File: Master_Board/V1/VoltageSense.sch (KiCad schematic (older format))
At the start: 3 parts

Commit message: git modify Master_board
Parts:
- removed U?: OP-AMP, F, symbol OP-AMP
- added C? (x4): 885012207098, Capacitors:C0805, symbol 885012207098
- added C? (x6): 885012207080, Capacitors:C0805, symbol 885012207080
- added D?: Diode, F, symbol Diode
- added J? (x2): 649002227222, Connectors:649002227222, symbol 649002227222
- added R? (x10): RC0805JR-0710KL, Resistors:R0805, symbol RC0805JR-0710KL
- added R? (x2): RC0805JR-071ML, Resistors:R0805, symbol RC0805JR-071ML
- added U? (x2): ACPL-C87A-500E, F, symbol ACPL-C87A-500E
- added U? (x2): LMV321RILT, IC:SOT-23-5, symbol LMV321RILT
- added U?: NCS1S2405SC, IC:MSOP-8-EP, symbol NCS1S2405SC
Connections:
- net labels added: 12V, 3.3V, 5V, 5V_ISO, BP-HV+, BP-HV-, BP_VSense, DGND, MPPT-HV+, MPPT-HV-, MPPT_VSense, VSense_EN
- net labels removed: HV+, HV-
- wire segments 2 -> 100
- no-connect marks 2 -> 4
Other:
- note added: "TODO: LC filter + control"
- moved on the sheet: J?

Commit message: Add filter in VoltageSense
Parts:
- added C?: 885012207075, Capacitors:C0805, symbol 885012207075
- added L?: RLB0608-471KL, Inductors:RLB0608, symbol RLB0608-471KL
- added R?: RC0805JR-07470RL, Resistors:R0805, symbol RC0805JR-07470RL
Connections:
- wire segments 100 -> 129
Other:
- note added: "Isolated"
- note removed: "TODO: LC filter + control"

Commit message: Add page LedDriver
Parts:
- gave numbers to parts that had none: 35
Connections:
- wire segments 129 -> 106

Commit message: Modify MasterBoard.sch
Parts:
- removed D801: Diode, F, symbol Diode
- removed R809, R810, R812, R813: RC0805JR-0710KL, Resistors:R0805, symbol RC0805JR-0710KL
- added D?: SD0805S020S1R0, Diodes:Diode_0805, symbol SD0805S020S1R0
- added R? (x4): RC0805JR-0715KL, Resistors:R0805, symbol RC0805JR-0715KL
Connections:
- wire segments 106 -> 104

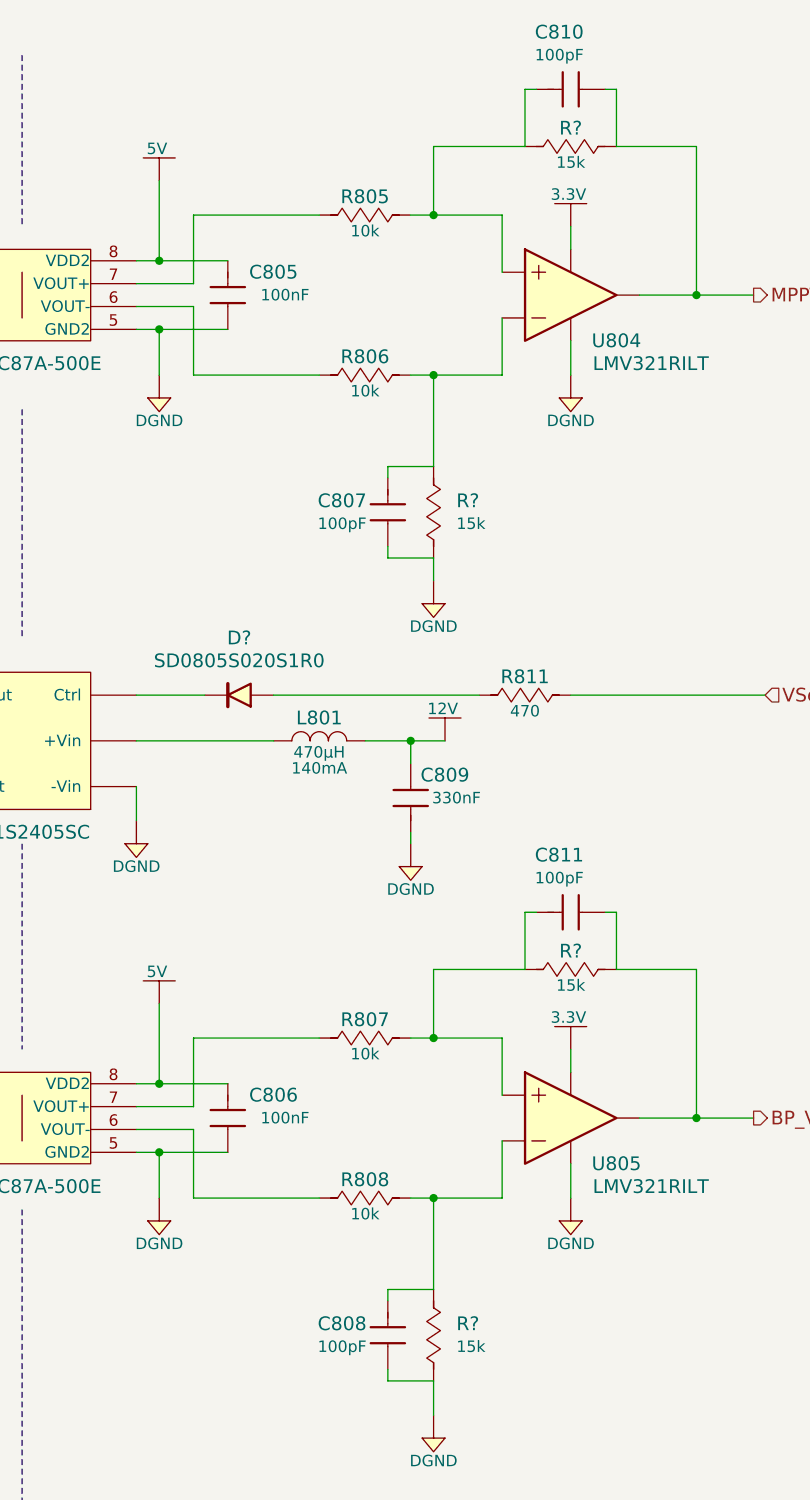
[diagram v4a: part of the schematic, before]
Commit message: Add page LEDDriver.sch
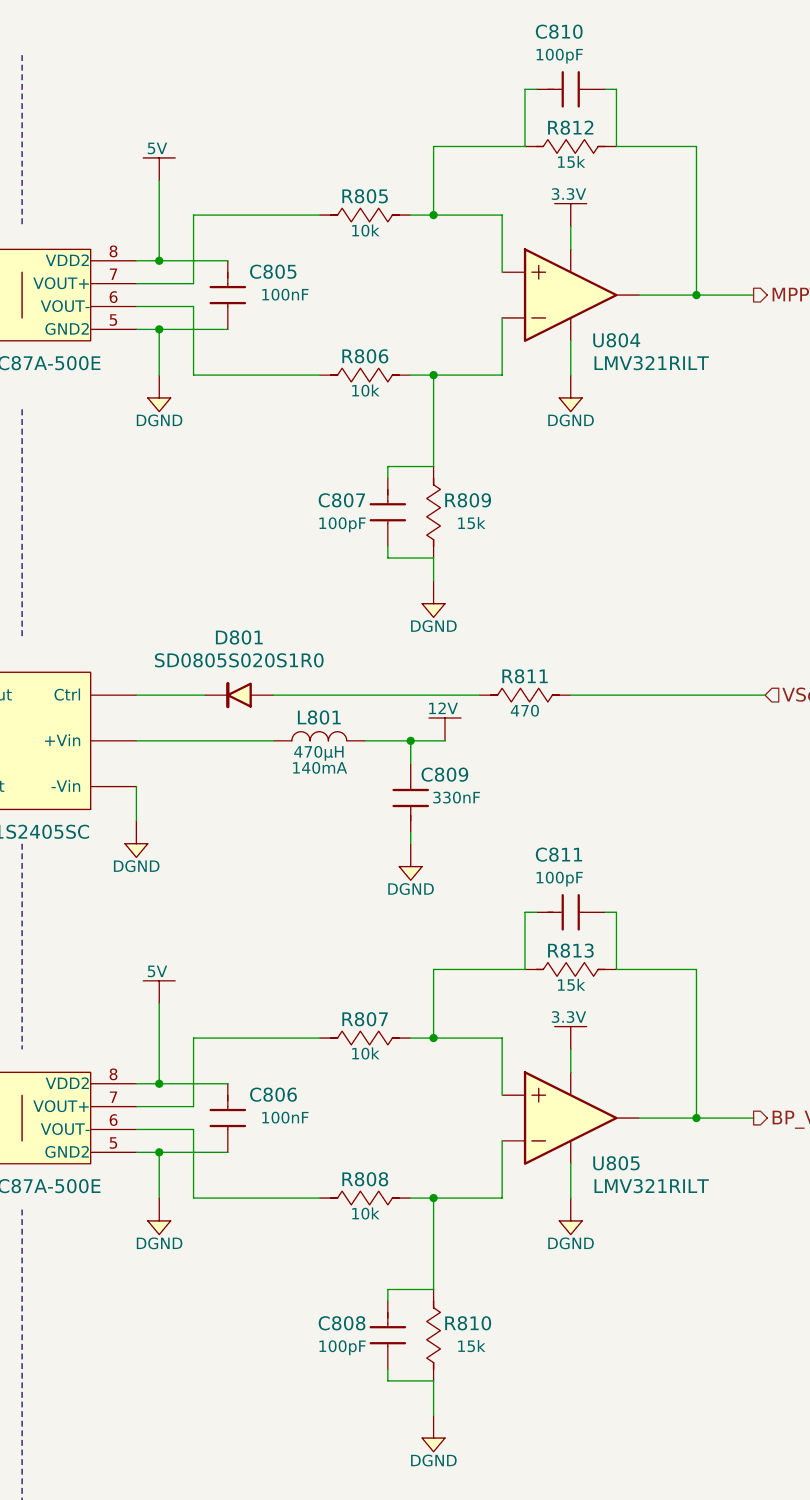
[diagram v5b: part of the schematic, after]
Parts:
- U801, U803: footprint F -> IC:SSO-8
- gave numbers to parts that had none: 5
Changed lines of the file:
@@
 EESchema Schematic File Version 2
-LIBS:Master_Board-rescue
 LIBS:ADC
 LIBS:Amplifiers
@@
 NoConn ~ 2100 5950
 $Comp
-L ACPL-C87A-500E U803
-U 1 1 5949C11F
-P 4900 5500
-F 0 "U803" H 4650 6000 60  0000 C CNN
-F 1 "ACPL-C87A-500E" H 4900 5400 60  0000 C CNN
-F 2 "F" H 4900 4600 60  0001 C CNN
-F 3 "https://docs.broadcom.com/docs/AV02-3563EN" H 4900 4500 60  0001 C CNN
-F 4 "Digikey" H 4900 5100 60  0001 C CNN "Supplier"
-F 5 "516-3140-1-ND" H 4900 5000 60  0001 C CNN "Supplier Part Number"
-F 6 "Broadcom Limited" H 4900 4900 60  0001 C CNN "Manufacturer"
-F 7 "ACPL-C87A-500E" H 4900 4800 60  0001 C CNN "Manufacturer Part Number"
-F 8 "Precision Optically Isolated Voltage Sensor" H 4900 4700 60  0001 C CNN "Description"
-	1    4900 5500
-	1    0    0    -1
-$EndComp
-$Comp
-L DGND #PWR802
+L DGND #PWR087
 U 1 1 5949C551
 P 4300 5700
-F 0 "#PWR802" H 4300 5530 50  0001 C CNN
+F 0 "#PWR087" H 4300 5530 50  0001 C CNN
 F 1 "DGND" H 4300 5600 50  0000 C CNN
 F 2 "" H 4300 5800 60  0000 C CNN
@@
 $EndComp
 $Comp
-L DGND #PWR808
+L DGND #PWR088
 U 1 1 5949C56B
 P 5500 5750
-F 0 "#PWR808" H 5500 5580 50  0001 C CNN
+F 0 "#PWR088" H 5500 5580 50  0001 C CNN
 F 1 "DGND" H 5500 5650 50  0000 C CNN
 F 2 "" H 5500 5850 60  0000 C CNN
@@
 BP_VSense
 $Comp
-L DGND #PWR816
+L DGND #PWR089
 U 1 1 5949FCE5
 P 7300 5750
-F 0 "#PWR816" H 7300 5580 50  0001 C CNN
+F 0 "#PWR089" H 7300 5580 50  0001 C CNN
 F 1 "DGND" H 7300 5650 50  0000 C CNN
 F 2 "" H 7300 5850 60  0000 C CNN
@@
 $EndComp
 $Comp
-L DGND #PWR811
+L DGND #PWR090
 U 1 1 594A0EB3
 P 6700 6700
-F 0 "#PWR811" H 6700 6530 50  0001 C CNN
+F 0 "#PWR090" H 6700 6530 50  0001 C CNN
 F 1 "DGND" H 6700 6600 50  0000 C CNN
 F 2 "" H 6700 6800 60  0000 C CNN
@@
 $EndComp
 $Comp
-L 5V #PWR807
+L 5V #PWR091
 U 1 1 594A3B0E
 P 5500 4800
-F 0 "#PWR807" H 5500 4650 50  0001 C CNN
+F 0 "#PWR091" H 5500 4650 50  0001 C CNN
 F 1 "5V" H 5490 4940 50  0000 C CNN
 F 2 "" H 5500 4800 60  0000 C CNN
@@
 $EndComp
 $Comp
-L 3.3V #PWR815
+L 3.3V #PWR092
 U 1 1 594A4CD5
 P 7300 5000
-F 0 "#PWR815" H 7300 4850 50  0001 C CNN
+F 0 "#PWR092" H 7300 4850 50  0001 C CNN
 F 1 "3.3V" H 7290 5140 50  0000 C CNN
 F 2 "" H 7300 5000 60  0000 C CNN
@@
 $EndComp
 $Comp
-L DGND #PWR803
+L DGND #PWR093
 U 1 1 594A764A
 P 4400 4100
-F 0 "#PWR803" H 4400 3930 50  0001 C CNN
+F 0 "#PWR093" H 4400 3930 50  0001 C CNN
 F 1 "DGND" H 4400 4000 50  0000 C CNN
 F 2 "" H 4400 4200 60  0000 C CNN
@@
 $EndComp
 $Comp
-L DGND #PWR804
+L DGND #PWR094
 U 1 1 594A76E3
 P 5400 4100
-F 0 "#PWR804" H 5400 3930 50  0001 C CNN
+F 0 "#PWR094" H 5400 3930 50  0001 C CNN
 F 1 "DGND" H 5400 4000 50  0000 C CNN
 F 2 "" H 5400 4200 60  0000 C CNN
@@
 $EndComp
 $Comp
-L 12V #PWR812
+L 12V #PWR095
 U 1 1 594A78A1
 P 6750 3650
-F 0 "#PWR812" H 6750 3500 50  0001 C CNN
+F 0 "#PWR095" H 6750 3500 50  0001 C CNN
 F 1 "12V" H 6740 3790 50  0000 C CNN
 F 2 "" H 6750 3650 60  0000 C CNN
@@
 NoConn ~ 2100 2350
 $Comp
-L ACPL-C87A-500E U801
-U 1 1 594A8989
-P 4900 1900
-F 0 "U801" H 4650 2400 60  0000 C CNN
-F 1 "ACPL-C87A-500E" H 4900 1800 60  0000 C CNN
-F 2 "F" H 4900 1000 60  0001 C CNN
-F 3 "https://docs.broadcom.com/docs/AV02-3563EN" H 4900 900 60  0001 C CNN
-F 4 "Digikey" H 4900 1500 60  0001 C CNN "Supplier"
-F 5 "516-3140-1-ND" H 4900 1400 60  0001 C CNN "Supplier Part Number"
-F 6 "Broadcom Limited" H 4900 1300 60  0001 C CNN "Manufacturer"
-F 7 "ACPL-C87A-500E" H 4900 1200 60  0001 C CNN "Manufacturer Part Number"
-F 8 "Precision Optically Isolated Voltage Sensor" H 4900 1100 60  0001 C CNN "Description"
-	1    4900 1900
-	1    0    0    -1
-$EndComp
-$Comp
-L DGND #PWR801
+L DGND #PWR096
 U 1 1 594A898F
 P 4300 2100
-F 0 "#PWR801" H 4300 1930 50  0001 C CNN
+F 0 "#PWR096" H 4300 1930 50  0001 C CNN
 F 1 "DGND" H 4300 2000 50  0000 C CNN
 F 2 "" H 4300 2200 60  0000 C CNN
@@
 $EndComp
 $Comp
-L DGND #PWR806
+L DGND #PWR097
 U 1 1 594A8995
 P 5500 2150
-F 0 "#PWR806" H 5500 1980 50  0001 C CNN
+F 0 "#PWR097" H 5500 1980 50  0001 C CNN
 F 1 "DGND" H 5500 2050 50  0000 C CNN
 F 2 "" H 5500 2250 60  0000 C CNN
@@
 MPPT_VSense
 $Comp
-L DGND #PWR814
+L DGND #PWR098
 U 1 1 594A8A41
 P 7300 2150
-F 0 "#PWR814" H 7300 1980 50  0001 C CNN
+F 0 "#PWR098" H 7300 1980 50  0001 C CNN
 F 1 "DGND" H 7300 2050 50  0000 C CNN
 F 2 "" H 7300 2250 60  0000 C CNN
@@
 $EndComp
 $Comp
-L DGND #PWR810
+L DGND #PWR099
 U 1 1 594A8A81
 P 6700 3050
-F 0 "#PWR810" H 6700 2880 50  0001 C CNN
+F 0 "#PWR099" H 6700 2880 50  0001 C CNN
 F 1 "DGND" H 6700 2950 50  0000 C CNN
 F 2 "" H 6700 3150 60  0000 C CNN
@@
 $EndComp
 $Comp
-L 5V #PWR805
+L 5V #PWR0100
 U 1 1 594A8A88
 P 5500 1200
-F 0 "#PWR805" H 5500 1050 50  0001 C CNN
+F 0 "#PWR0100" H 5500 1050 50  0001 C CNN
 F 1 "5V" H 5490 1340 50  0000 C CNN
 F 2 "" H 5500 1200 60  0000 C CNN
@@
 $EndComp
 $Comp
-L 3.3V #PWR813
+L 3.3V #PWR0101
 U 1 1 594A8A8E
 P 7300 1400
-F 0 "#PWR813" H 7300 1250 50  0001 C CNN
+F 0 "#PWR0101" H 7300 1250 50  0001 C CNN
 F 1 "3.3V" H 7290 1540 50  0000 C CNN
 F 2 "" H 7300 1400 60  0000 C CNN
@@
 Connection ~ 6600 3650
 $Comp
-L DGND #PWR809
+L DGND #PWR0102
 U 1 1 59486B2F
 P 6600 4200
-F 0 "#PWR809" H 6600 4030 50  0001 C CNN
+F 0 "#PWR0102" H 6600 4030 50  0001 C CNN
 F 1 "DGND" H 6600 4100 50  0000 C CNN
 F 2 "" H 6600 4300 60  0000 C CNN
@@
 Isolated
 $Comp
-L SD0805S020S1R0 D?
+L SD0805S020S1R0 D801
 U 1 1 594E14E6
 P 5800 3450
-F 0 "D?" H 5750 3200 60  0000 C CNN
+F 0 "D801" H 5750 3200 60  0000 C CNN
 F 1 "SD0805S020S1R0" H 5750 3300 60  0000 C CNN
 F 2 "Diodes:Diode_0805" H 5800 2430 60  0001 C CNN
@@
 $EndComp
 $Comp
-L RC0805JR-0715KL R?
+L RC0805JR-0715KL R812
 U 1 1 59539105
 P 7300 1050
-F 0 "R?" H 7300 1130 60  0000 C CNN
+F 0 "R812" H 7300 1130 60  0000 C CNN
 F 1 "RC0805JR-0715KL" H 7300 750 50  0001 C CNN
 F 2 "Resistors:R0805" H 7300 150 30  0001 C CNN
@@
 $EndComp
 $Comp
-L RC0805JR-0715KL R?
+L RC0805JR-0715KL R813
 U 1 1 59539316
 P 7300 4650
-F 0 "R?" H 7300 4730 60  0000 C CNN
+F 0 "R813" H 7300 4730 60  0000 C CNN
 F 1 "RC0805JR-0715KL" H 7300 4350 50  0001 C CNN
 F 2 "Resistors:R0805" H 7300 3750 30  0001 C CNN
@@
 $EndComp
 $Comp
-L RC0805JR-0715KL R?
+L RC0805JR-0715KL R809
 U 1 1 595393DC
 P 6700 2650
-F 0 "R?" V 6650 2800 60  0000 C CNN
+F 0 "R809" V 6650 2800 60  0000 C CNN
 F 1 "RC0805JR-0715KL" H 6700 2350 50  0001 C CNN
 F 2 "Resistors:R0805" H 6700 1750 30  0001 C CNN
@@
 $EndComp
 $Comp
-L RC0805JR-0715KL R?
+L RC0805JR-0715KL R810
 U 1 1 5953A5C1
 P 6700 6250
-F 0 "R?" V 6650 6400 60  0000 C CNN
+F 0 "R810" V 6650 6400 60  0000 C CNN
 F 1 "RC0805JR-0715KL" H 6700 5950 50  0001 C CNN
 F 2 "Resistors:R0805" H 6700 5350 30  0001 C CNN
@@
 	0    1    1    0
 $EndComp
+$Comp
+L ACPL-C87A-500E U801
+U 1 1 59616333
+P 4900 1900
+F 0 "U801" H 4650 2400 60  0000 C CNN
+F 1 "ACPL-C87A-500E" H 4900 1800 60  0000 C CNN
+F 2 "IC:SSO-8" H 4900 1000 60  0001 C CNN
+F 3 "https://docs.broadcom.com/docs/AV02-3563EN" H 4900 900 60  0001 C CNN
+F 4 "Digikey" H 4900 1500 60  0001 C CNN "Supplier"
+F 5 "516-3140-1-ND" H 4900 1400 60  0001 C CNN "Supplier Part Number"
+F 6 "Broadcom Limited" H 4900 1300 60  0001 C CNN "Manufacturer"
+F 7 "ACPL-C87A-500E" H 4900 1200 60  0001 C CNN "Manufacturer Part Number"
+F 8 "Precision Optically Isolated Voltage Sensor" H 4900 1100 60  0001 C CNN "Description"
+	1    4900 1900
+	1    0    0    -1
+$EndComp
+$Comp
+L ACPL-C87A-500E U803
+U 1 1 59616A29
+P 4900 5500
+F 0 "U803" H 4650 6000 60  0000 C CNN
+F 1 "ACPL-C87A-500E" H 4900 5400 60  0000 C CNN
+F 2 "IC:SSO-8" H 4900 4600 60  0001 C CNN
+F 3 "https://docs.broadcom.com/docs/AV02-3563EN" H 4900 4500 60  0001 C CNN
+F 4 "Digikey" H 4900 5100 60  0001 C CNN "Supplier"
+F 5 "516-3140-1-ND" H 4900 5000 60  0001 C CNN "Supplier Part Number"
+F 6 "Broadcom Limited" H 4900 4900 60  0001 C CNN "Manufacturer"
+F 7 "ACPL-C87A-500E" H 4900 4800 60  0001 C CNN "Manufacturer Part Number"
+F 8 "Precision Optically Isolated Voltage Sensor" H 4900 4700 60  0001 C CNN "Description"
+	1    4900 5500
+	1    0    0    -1
+$EndComp
 $EndSCHEMATC
